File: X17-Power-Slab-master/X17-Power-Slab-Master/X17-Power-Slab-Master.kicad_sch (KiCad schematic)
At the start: 15 parts, among them J1 Conn_01x12_Pin, J2 ET60T-D04-3-08-D04-X-R1-S, J3 796636-6, Q2 TSM340N06CP ROG

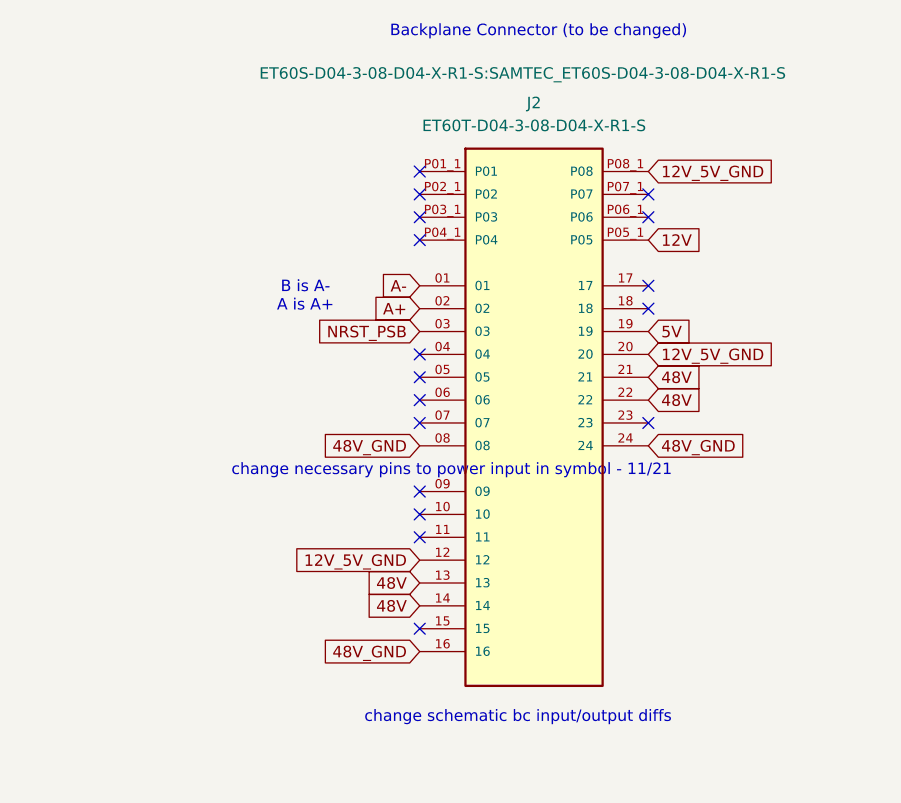
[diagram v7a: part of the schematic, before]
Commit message: silkscreen + pinout fixes
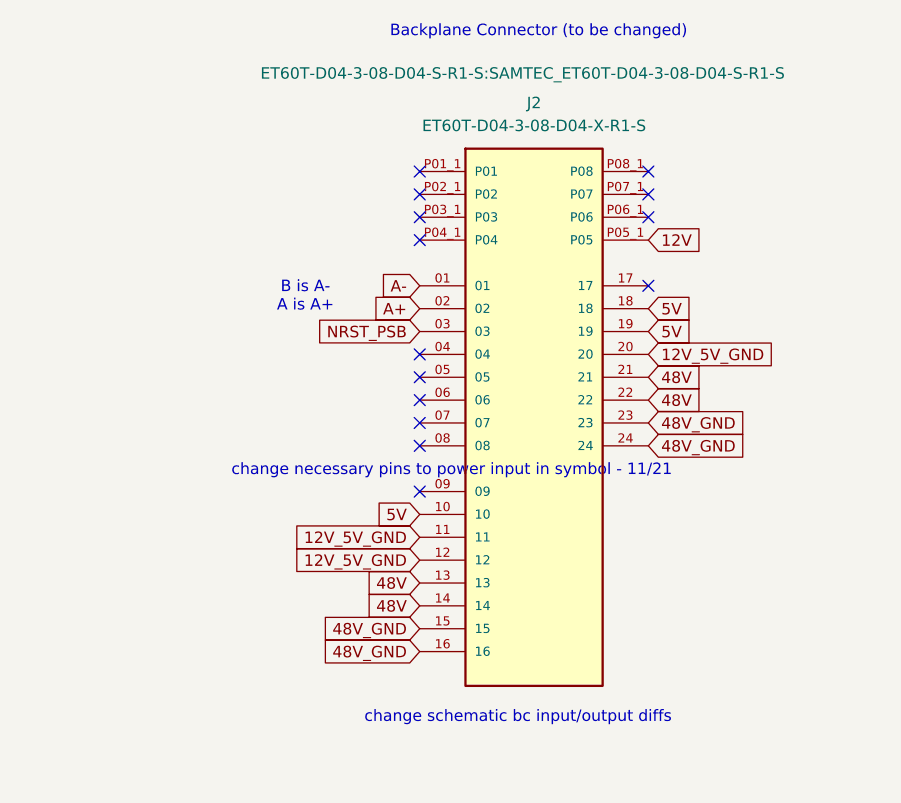
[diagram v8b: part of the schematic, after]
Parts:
- J2: footprint ET60S-D04-3-08-D04-X-R1-S:SAMTEC_ET60S-D04-3-08-D04-X-R1-S -> ET60T-D04-3-08-D04-S-R1-S:SAMTEC_ET60T-D04-3-08-D04-S-R1-S
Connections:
- net 12V_5V_GND: now also J2.11; no longer J2.P08_1 (P08)
- net 48V_GND: now also J2.15, J2.23; no longer J2.08
- net 5V: now also J2.10, J2.18
- no-connect marks 19 -> 16
